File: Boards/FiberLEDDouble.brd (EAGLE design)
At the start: 16.5 x 7.6 mm, 5 parts, among them U1 WS2812, U2 WS2812

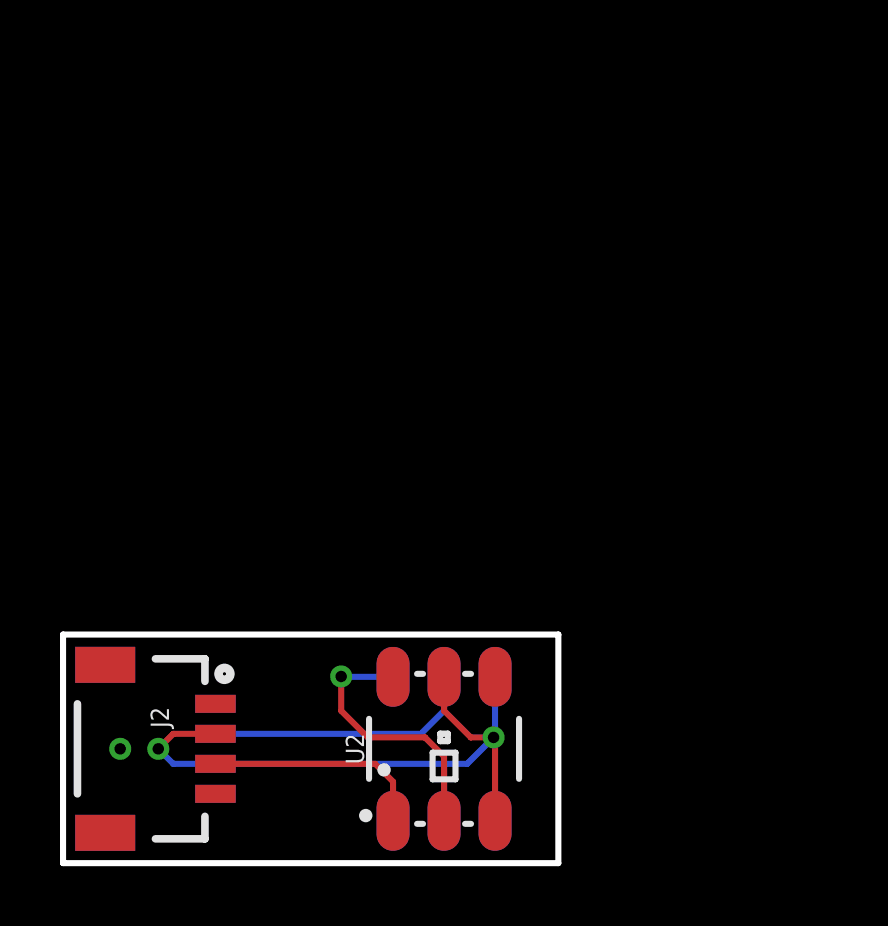
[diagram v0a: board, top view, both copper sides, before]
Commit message: added and ordered LEDs
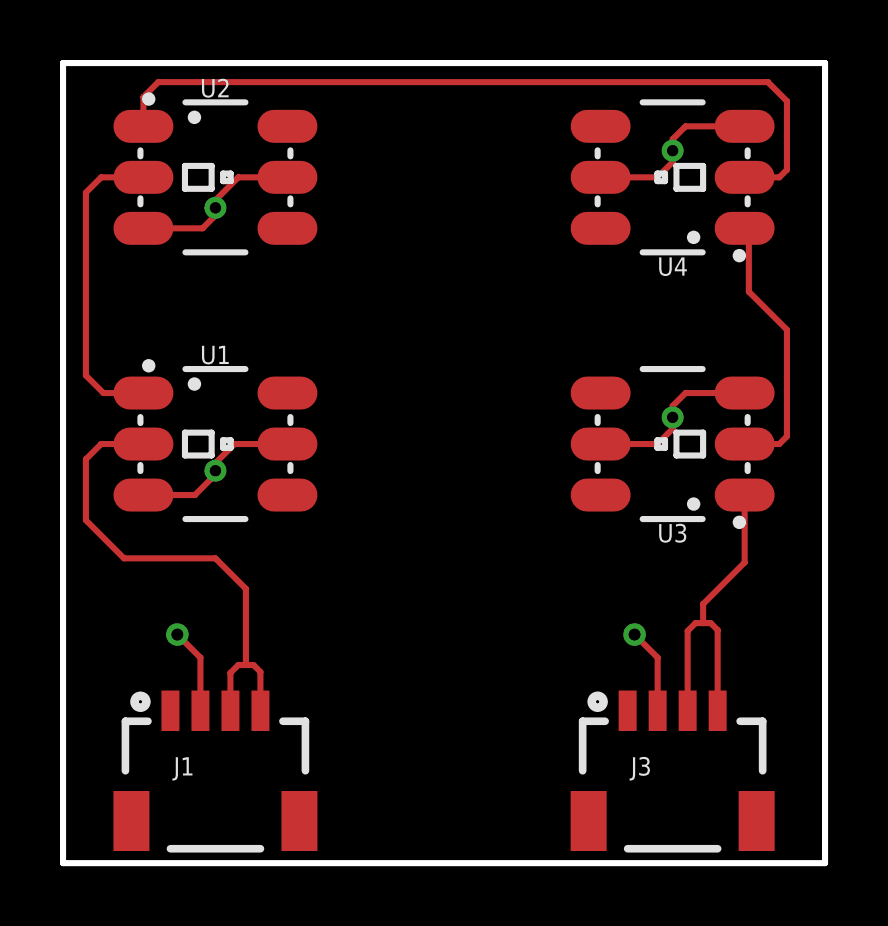
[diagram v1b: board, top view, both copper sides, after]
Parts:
- removed J2: (no value), SparkFun-Connectors:1X04_1MM_RA
- added J3: (no value), SparkFun-Connectors:1X04_1MM_RA
- added U3, U4: WS2812, SparkFun-LED:LED-TRICOLOR-5050-IC
- moved U2 20.5 mm to (5.08, 22.9), turned to 0 degrees
- moved U1 12.7 mm to (5.08, 14.0), flipped to the top, turned to 0 degrees
- moved J1 1.27 mm to (5.08, 5.08), flipped to the top, turned to 0 degrees
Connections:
- new net N$2: U3.2, U4.1
- new net N$4: J3.3, J3.4, U3.1
- net 5V: now also J3.2, U3.3, U3.5, U4.3, U4.5; no longer J2.2
- net GND: now also J3.1, U3.6, U4.6; no longer J2.1
- net N$1: now also J1.4
- net N$3: now also U4.2; no longer J2.3
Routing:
- net N$3: track 7.47 -> 26.7 mm
- net N$4: track 0.00 -> 11.4 mm
- net N$2: track 0.00 -> 9.04 mm
- net N$1: track 9.07 -> 16.7 mm
- net 5V: track 23.7 -> 29.1 mm, vias 2 -> 6
- net N$5: track 9.08 -> 10.4 mm, vias 1 -> 0
- added copper zone on layer 16, net 5V
- removed copper zone on layer 16, net GND
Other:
- board size 16.5 x 7.6 mm -> 25.4 x 26.7 mm
